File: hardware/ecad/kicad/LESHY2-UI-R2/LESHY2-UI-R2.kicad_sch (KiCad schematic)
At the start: 0 parts

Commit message: Review R2 startup and fault-display sequencing
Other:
- sheet UI_10_S3_DISPLAY_TOUCH ports: added S3_RESET_KILL_GATE; removed C5_SERVICE_PATH_ACK
- sheet UI_40_INTERBOARD_M1 ports: added S3_RESET_KILL_GATE; removed none
- sheet UI_50_FRONT_POWER_SAFETY ports: added S3_RESET_KILL_GATE; removed none

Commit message: Review R2 power transitions and watchdog
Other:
- sheet UI_11_STORAGE_CONTROLS_INDICATORS ports: added FAULT_KILL; removed FAULT_ASSERT_N
- sheet UI_40_INTERBOARD_M1 ports: added FAULT_KILL; removed none

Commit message: Mount display through direct UI-board ZIF
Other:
- sheet UI_10_S3_DISPLAY_TOUCH ports: added LCD_LEDA_PROTECTED, LCD_LEDK, LCD_TOUCH_INT_RAW_N; removed LCD_DB0, LCD_DB1, LCD_DB2, LCD_DB3, LCD_DB4, LCD_DB5, LCD_DB6, LCD_DB7, LCD_DC, LCD_WR_N
- sheet UI_11_STORAGE_CONTROLS_INDICATORS ports: added LCD_LEDA_PROTECTED, LCD_LEDK, LCD_TOUCH_INT_RAW_N; removed LCD_DB0, LCD_DB1, LCD_DB2, LCD_DB3, LCD_DB4, LCD_DB5, LCD_DB6, LCD_DB7, LCD_DC, LCD_TE, LCD_WR_N
- sheet UI_30_HUB_RP_CORE_SERVICE ports: added none; removed LCD_TE

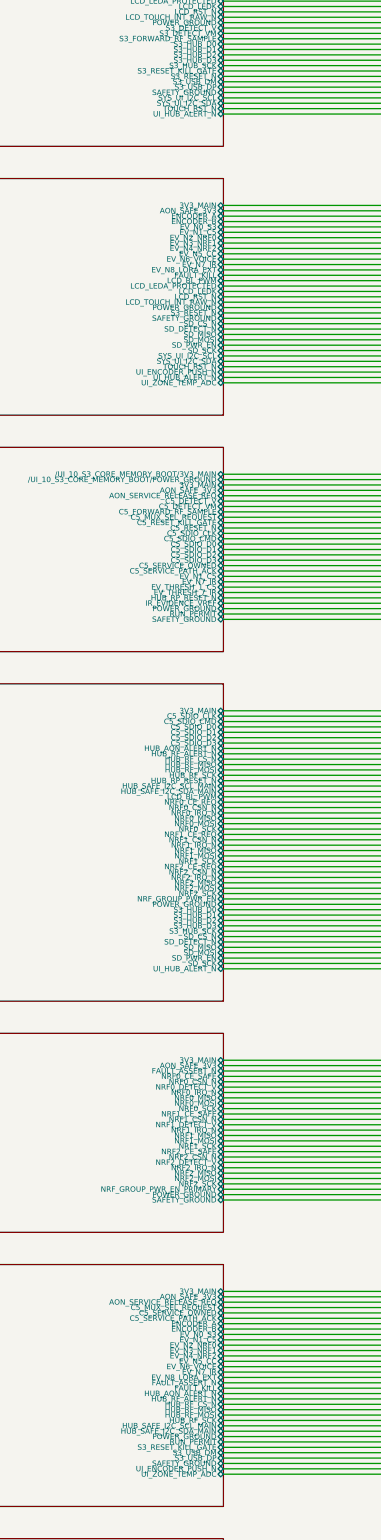
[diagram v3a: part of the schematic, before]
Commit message: Bind H6 RF and USB routing geometry
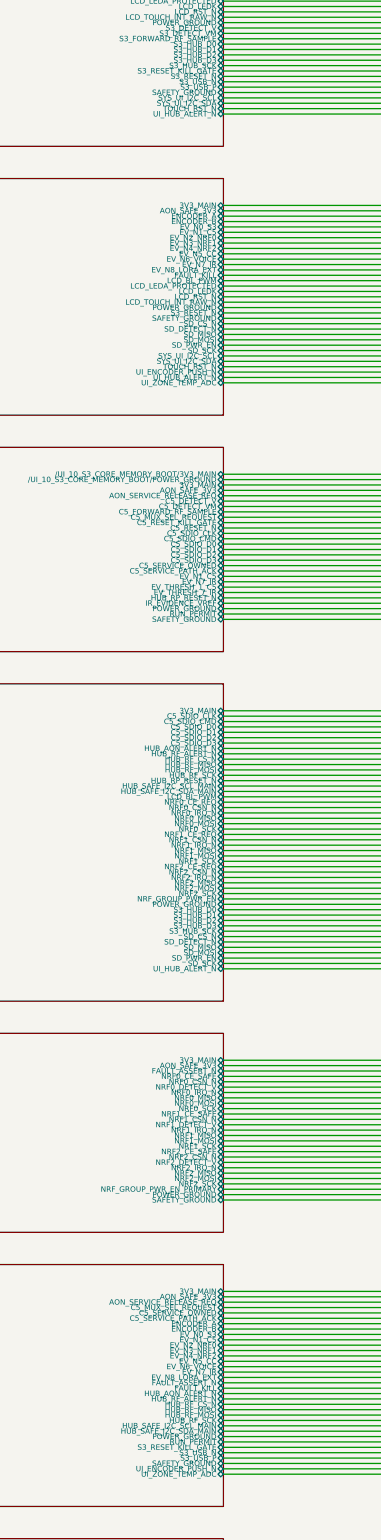
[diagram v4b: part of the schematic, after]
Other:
- sheet UI_10_S3_DISPLAY_TOUCH ports: added S3_USB_N, S3_USB_P; removed S3_USB_DM, S3_USB_DP
- sheet UI_40_INTERBOARD_M1 ports: added S3_USB_N, S3_USB_P; removed S3_USB_DM, S3_USB_DP
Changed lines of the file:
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@@
 			(effects (font (size 1.27 1.27)))
 		)
-		(pin "S3_USB_DM" bidirectional
+		(pin "S3_USB_N" bidirectional
 			(at 274.32 55.88 0)
 			(effects (font (size 1.27 1.27)))
 		)
-		(pin "S3_USB_DP" bidirectional
+		(pin "S3_USB_P" bidirectional
 			(at 274.32 57.15 0)
 			(effects (font (size 1.27 1.27)))
@@
 			(effects (font (size 1.27 1.27)))
 		)
-		(pin "S3_USB_DM" bidirectional
+		(pin "S3_USB_N" bidirectional
 			(at 274.32 379.73 0)
 			(effects (font (size 1.27 1.27)))
 		)
-		(pin "S3_USB_DP" bidirectional
+		(pin "S3_USB_P" bidirectional
 			(at 274.32 381.00 0)
 			(effects (font (size 1.27 1.27)))

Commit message: Canonicalize physical ground anchors
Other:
- sheet UI_10_S3_DISPLAY_TOUCH ports: added none; removed /UI_10_S3_CORE_MEMORY_BOOT/POWER_GROUND, SAFETY_GROUND
- sheet UI_11_STORAGE_CONTROLS_INDICATORS ports: added none; removed SAFETY_GROUND
- sheet UI_20_C5_WIFI_IR_SERVICE ports: added none; removed /UI_10_S3_CORE_MEMORY_BOOT/POWER_GROUND, SAFETY_GROUND
- sheet UI_31_NRF24_X3_TX_EVIDENCE ports: added none; removed SAFETY_GROUND
- sheet UI_40_INTERBOARD_M1 ports: added none; removed SAFETY_GROUND
- sheet UI_50_FRONT_POWER_SAFETY ports: added POWER_GROUND; removed SAFETY_GROUND

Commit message: Correct SMA geometry and module power; bind verification to current boards
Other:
- sheet UI_10_S3_DISPLAY_TOUCH ports: added none; removed /UI_10_S3_CORE_MEMORY_BOOT/3V3_MAIN
- sheet UI_20_C5_WIFI_IR_SERVICE ports: added none; removed /UI_10_S3_CORE_MEMORY_BOOT/3V3_MAIN

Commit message: Repair C5 service mux controls without weakening hardware KILL
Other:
- sheet UI_20_C5_WIFI_IR_SERVICE ports: added FAULT_ASSERT_N; removed none
